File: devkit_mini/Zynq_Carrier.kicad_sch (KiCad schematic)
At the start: 0 parts

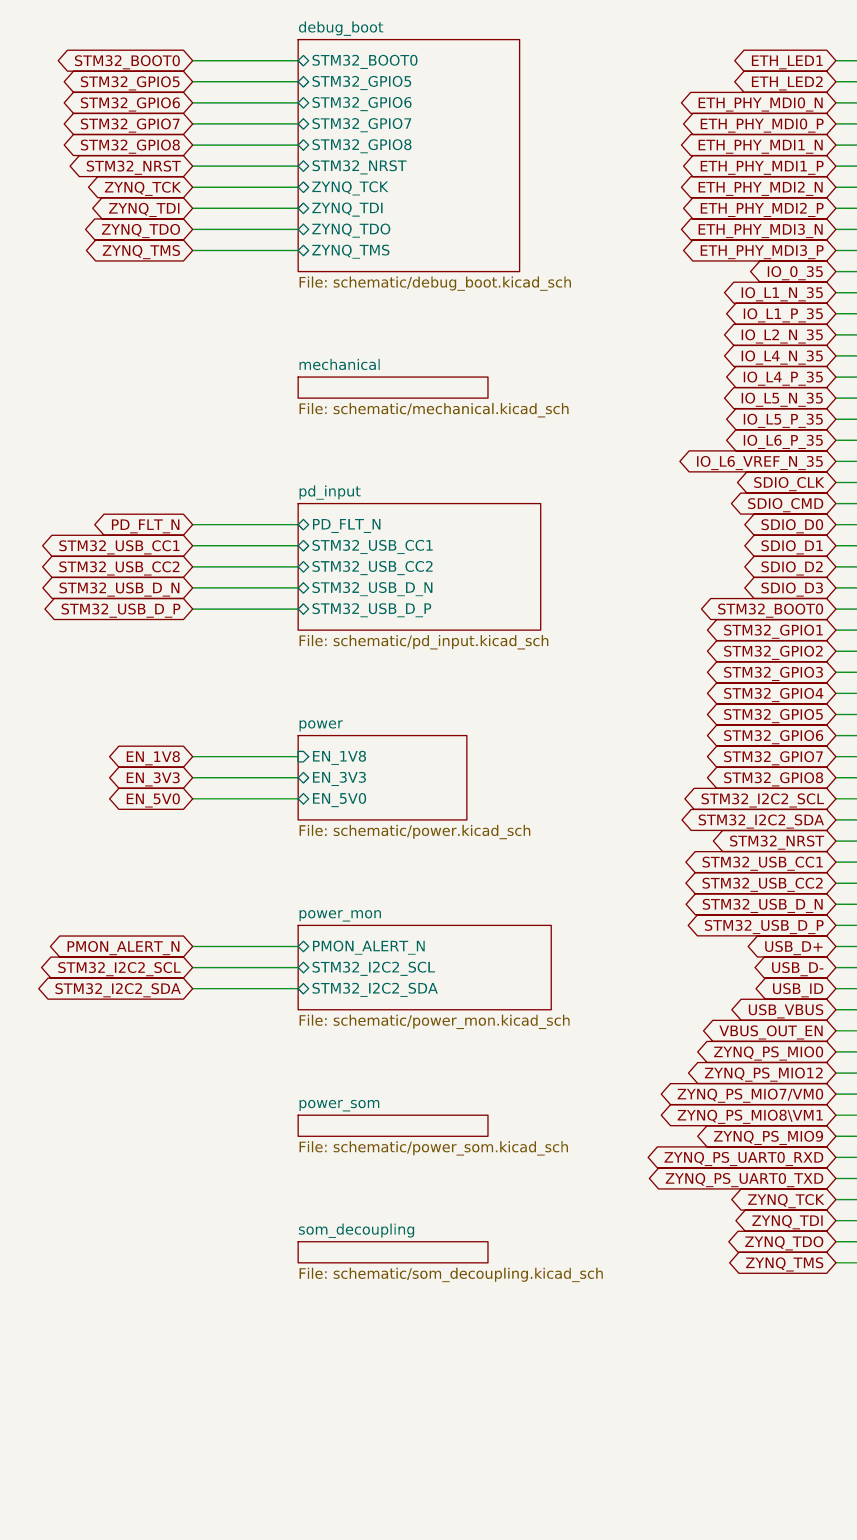
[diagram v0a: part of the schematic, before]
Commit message: feat(native): migrate schematic pipeline and fix devkit electrical coverage
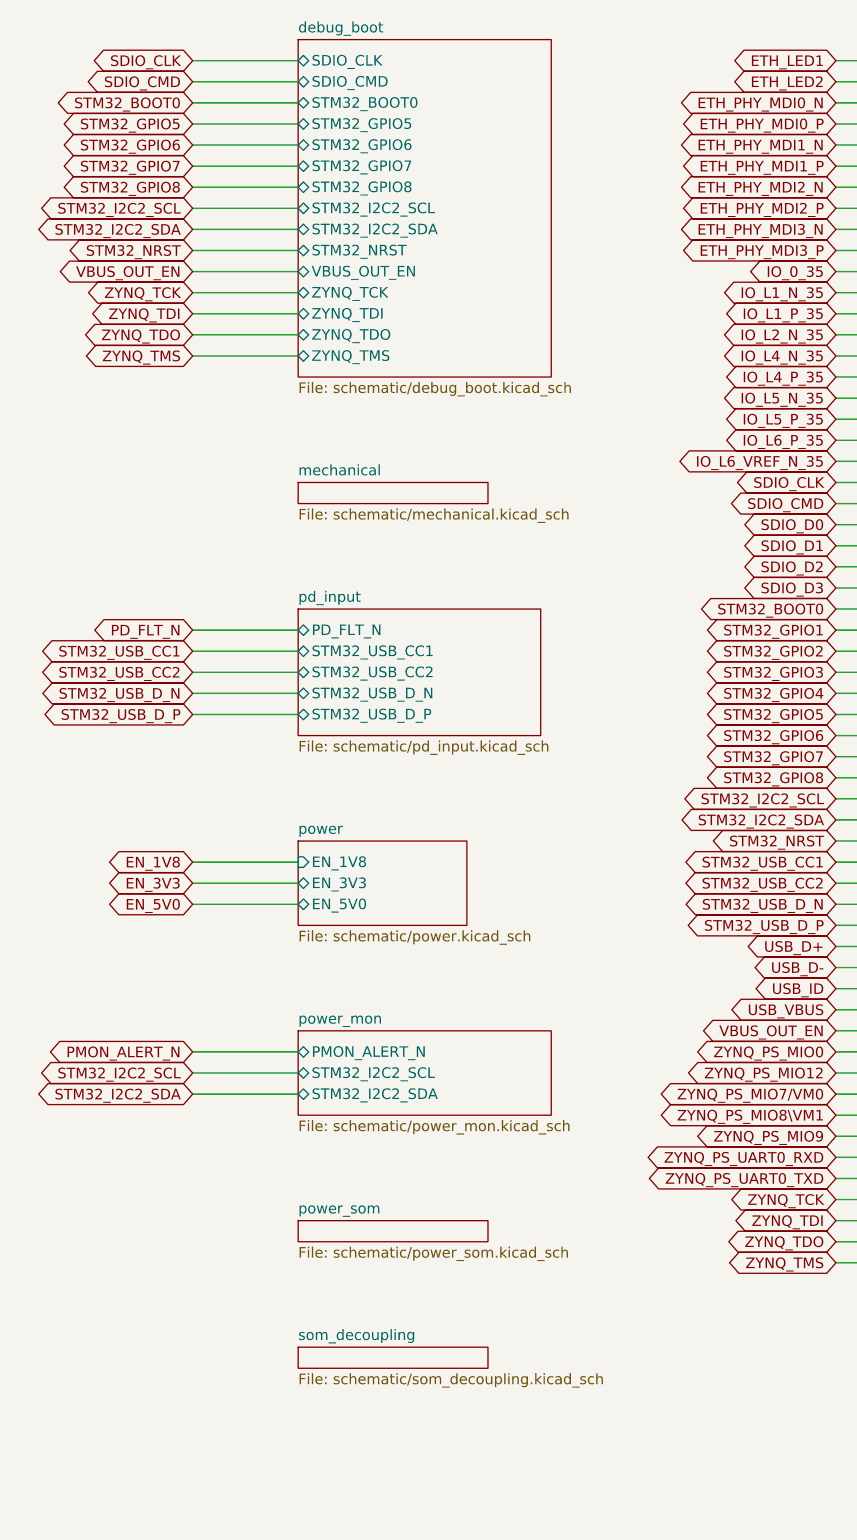
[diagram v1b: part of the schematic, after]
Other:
- sheet debug_boot ports: added SDIO_CLK, SDIO_CMD, STM32_I2C2_SCL, STM32_I2C2_SDA, VBUS_OUT_EN; removed none

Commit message: Publish current carrier and devkit placement release with fresh renders
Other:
- company: Zynq SoM Carrier -> Zynq SoM Devkit Mini
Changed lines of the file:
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@@
 	(title_block
 		(title "carrier board root")
-		(company "Zynq SoM Carrier")
+		(company "Zynq SoM Devkit Mini")
 		(comment 1 "Zynq_Carrier — generated by schgen (do not hand-edit)")
 	)
